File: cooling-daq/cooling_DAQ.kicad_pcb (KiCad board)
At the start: 2 copper layers, 30 x 50 mm, 51 parts, among them J1 Conn_02x10_Odd_Even, J7 USB_C_Receptacle_USB2.0_16P, Q1 2N7002, Q2 2N7002, SW1 SW_SPST, U1 STM32F103C8Tx, U2 AP2204K-ADJ, U3 AP2204K-ADJ, U4 SN65HVD256D, Y1 8M, Y2 32.768k

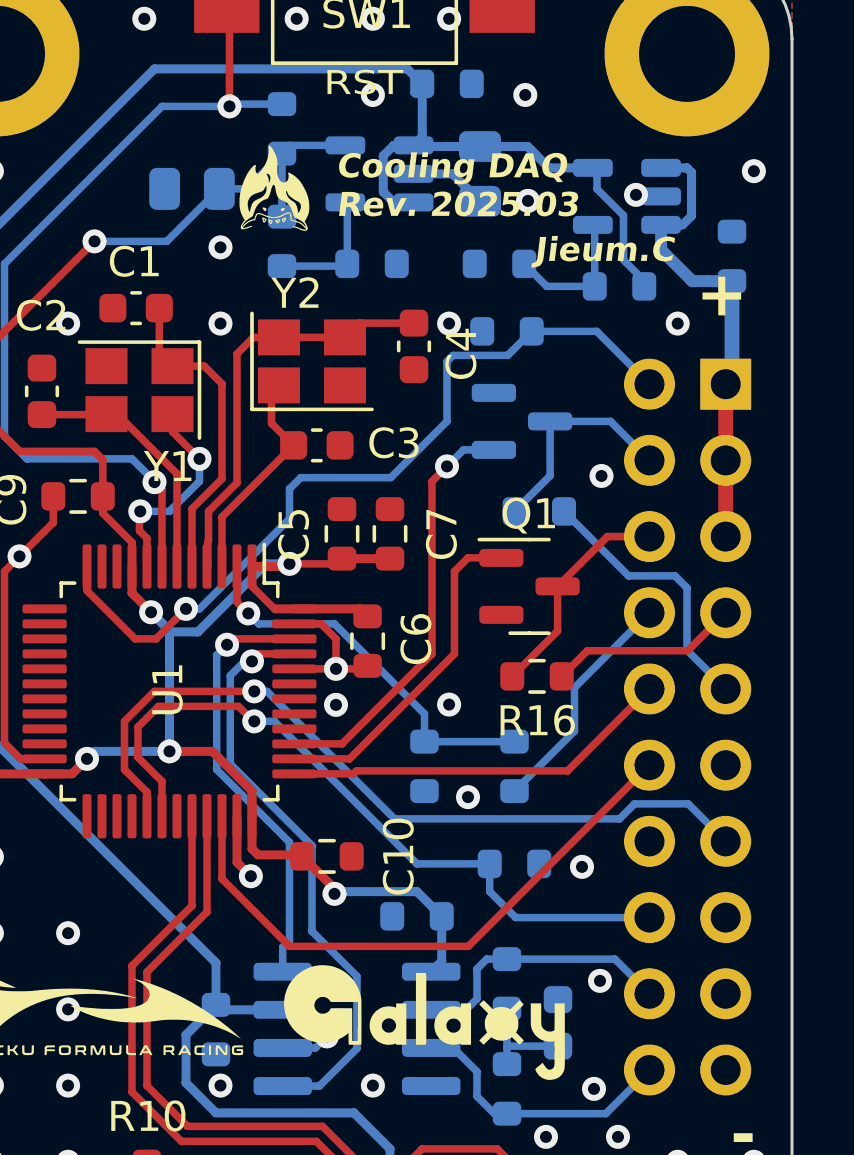
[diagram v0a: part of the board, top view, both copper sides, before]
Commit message: fix CAN IC, modify pump_PWR, fix Cu length label
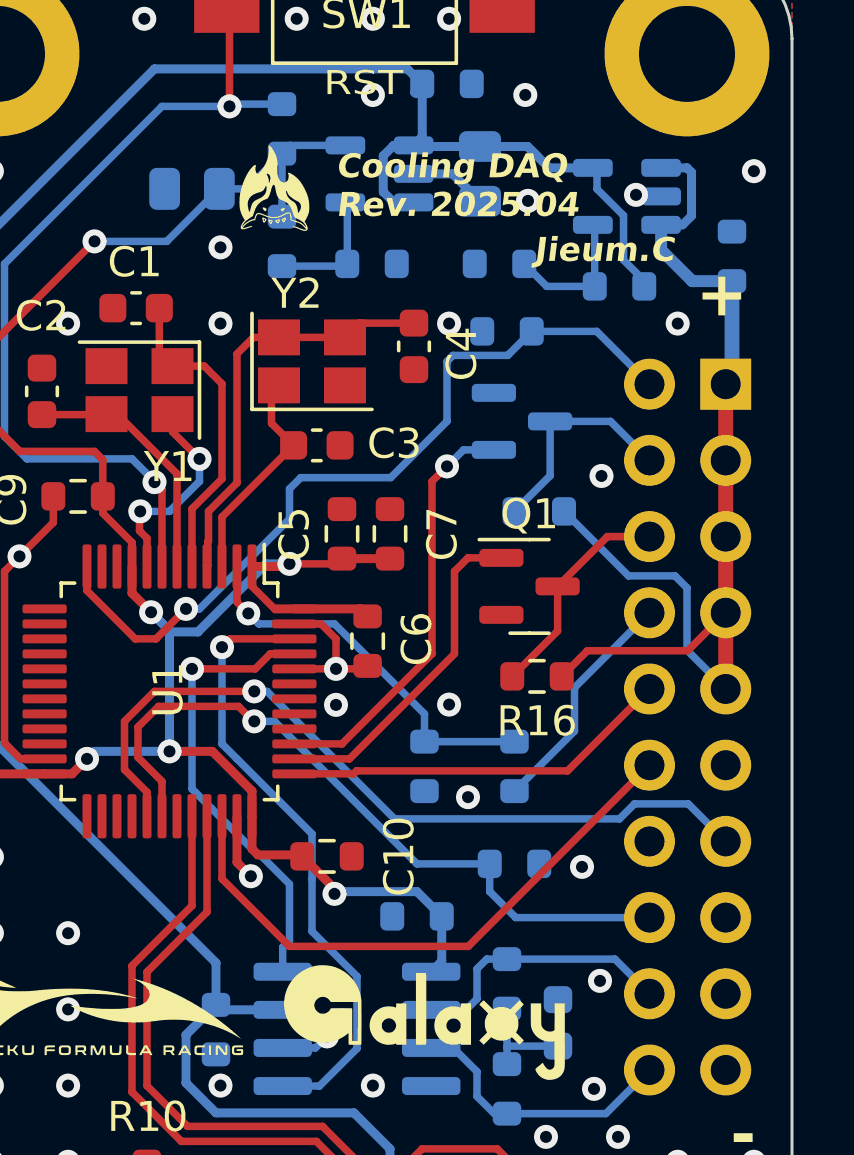
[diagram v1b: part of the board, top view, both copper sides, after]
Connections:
- J1 pad 7: PUMP_PWR -> VDC
- J1 pad 9: FAN_PWR -> VDC
- R14 pad 2: FAN_PWR -> VDC
- R16 pad 2: PUMP_PWR -> VDC
- U1 pad 45: CAN_TX -> CAN_RX
- U1 pad 46: CAN_RX -> CAN_TX
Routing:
- net VDC: track 15.9 -> 36.4 mm
- net FAN_PWR: track 9.06 -> 0.00 mm
- net PUMP_PWR: track 6.34 -> 0.00 mm
- net CAN_TX: track 19.6 -> 20.8 mm
- net CAN_RX: track 14.5 -> 15.2 mm
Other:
- board text added: "Cooling DAQ Rev. 2025.04"
- board text removed: "Cooling DAQ Rev. 2025.03"

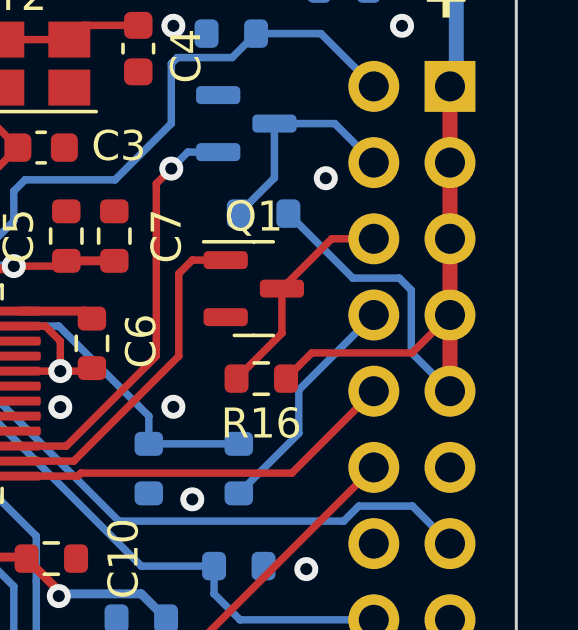
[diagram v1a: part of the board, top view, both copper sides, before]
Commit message: recover PUMP_PWR
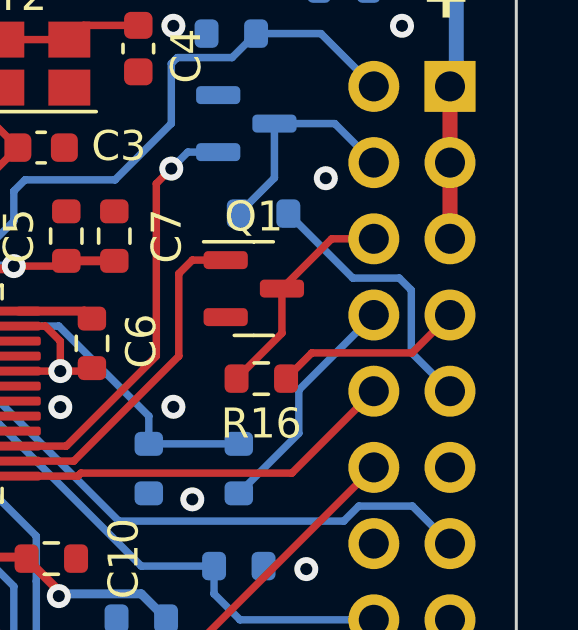
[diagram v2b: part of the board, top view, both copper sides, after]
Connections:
- J1 pad 7: VDC -> PUMP_PWR
- J1 pad 9: VDC -> FAN_PWR
- R14 pad 2: VDC -> FAN_PWR
- R16 pad 2: VDC -> PUMP_PWR
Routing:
- net VDC: track 36.4 -> 15.9 mm
- net FAN_PWR: track 0.00 -> 9.06 mm
- net PUMP_PWR: track 0.00 -> 6.34 mm
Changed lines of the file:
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@@
   (net 56 "unconnected-(J1-Pin_11-Pad11)")
   (net 57 "unconnected-(J1-Pin_14-Pad14)")
+  (net 58 "PUMP_PWR")
+  (net 59 "FAN_PWR")
   (footprint "MountingHole:MountingHole_3.2mm_M3_ISO14580_Pad" (layer "F.Cu")
     (at 158.5 140.5)
@@
       (net 54 "PUMP_PWM") (pintype "passive"))
     (pad "2" smd roundrect (at 0.825 0) (size 0.8 0.95) (layers "F.Cu" "F.Paste" "F.Mask") (roundrect_rratio 0.25)
-      (net 7 "VDC") (pintype "passive"))
+      (net 58 "PUMP_PWR") (pintype "passive"))
     (model "${KICAD6_3DMODEL_DIR}/Resistor_SMD.3dshapes/R_0603_1608Metric.wrl"
       (offset (xyz 0 0 0))
@@
       (net 54 "PUMP_PWM") (pinfunction "Pin_6") (pintype "passive"))
     (pad "7" thru_hole oval (at 0 -7.62 180) (size 1.7 1.7) (drill 1) (layers "*.Cu" "*.Mask")
-      (net 7 "VDC") (pinfunction "Pin_7") (pintype "passive"))
+      (net 58 "PUMP_PWR") (pinfunction "Pin_7") (pintype "passive"))
     (pad "8" thru_hole oval (at 2.54 -7.62 180) (size 1.7 1.7) (drill 1) (layers "*.Cu" "*.Mask")
       (net 13 "PT_signal") (pinfunction "Pin_8") (pintype "passive"))
     (pad "9" thru_hole oval (at 0 -10.16 180) (size 1.7 1.7) (drill 1) (layers "*.Cu" "*.Mask")
-      (net 7 "VDC") (pinfunction "Pin_9") (pintype "passive"))
+      (net 59 "FAN_PWR") (pinfunction "Pin_9") (pintype "passive"))
     (pad "10" thru_hole oval (at 2.54 -10.16 180) (size 1.7 1.7) (drill 1) (layers "*.Cu" "*.Mask")
       (net 10 "SYS_JTCK-SWCLK") (pinfunction "Pin_10") (pintype "passive"))
@@
       (net 55 "FAN_PWM") (pintype "passive"))
     (pad "2" smd roundrect (at 0.825 0) (size 0.8 0.95) (layers "B.Cu" "B.Paste" "B.Mask") (roundrect_rratio 0.25)
-      (net 7 "VDC") (pintype "passive"))
+      (net 59 "FAN_PWR") (pintype "passive"))
     (model "${KICAD6_3DMODEL_DIR}/Resistor_SMD.3dshapes/R_0603_1608Metric.wrl"
       (offset (xyz 0 0 0))
@@
   (segment (start 146.75 125.5) (end 146.825 125.425) (width 0.3) (layer "B.Cu") (net 6))
   (segment (start 141.25 120.75) (end 138.75 120.75) (width 0.3) (layer "B.Cu") (net 6))
-  (segment (start 155.180054 117.394946) (end 158.525054 117.394946) (width 0.25) (layer "F.Cu") (net 7))
-  (segment (start 154.325 118.25) (end 155.180054 117.394946) (width 0.25) (layer "F.Cu") (net 7))
-  (segment (start 159.79 116.13) (end 159.79 118.67) (width 0.5) (layer "F.Cu") (net 7))
-  (segment (start 158.525054 117.394946) (end 159.79 116.13) (width 0.25) (layer "F.Cu") (net 7))
-  (segment (start 159.79 113.59) (end 159.79 116.13) (width 0.5) (layer "F.Cu") (net 7))
   (segment (start 159.79 108.51) (end 159.79 113.59) (width 0.5) (layer "F.Cu") (net 7))
   (segment (start 158.65 102.899999) (end 158.349999 103.2) (width 0.3) (layer "B.Cu") (net 7))
   (segment (start 160 105.075) (end 160 108.3) (width 0.5) (layer "B.Cu") (net 7))
   (segment (start 160 108.3) (end 159.79 108.51) (width 0.25) (layer "B.Cu") (net 7))
-  (segment (start 156.55 114.9) (end 158.1 114.9) (width 0.25) (layer "B.Cu") (net 7))
   (segment (start 157.6375 104.0375) (end 158.675 105.075) (width 0.4) (layer "B.Cu") (net 7))
   (segment (start 158.5 101.3) (end 158.65 101.45) (width 0.3) (layer "B.Cu") (net 7))
   (segment (start 158.65 101.45) (end 158.65 102.899999) (width 0.3) (layer "B.Cu") (net 7))
-  (segment (start 158.1 114.9) (end 158.5 115.3) (width 0.25) (layer "B.Cu") (net 7))
-  (segment (start 158.5 117.38) (end 159.79 118.67) (width 0.25) (layer "B.Cu") (net 7))
   (segment (start 158.675 105.075) (end 159.5125 105.075) (width 0.4) (layer "B.Cu") (net 7))
   (segment (start 157.6375 101.3) (end 158.5 101.3) (width 0.3) (layer "B.Cu") (net 7))
   (segment (start 157.6375 103.2) (end 157.6375 104.0375) (width 0.4) (layer "B.Cu") (net 7))
-  (segment (start 154.4 112.75) (end 156.55 114.9) (width 0.25) (layer "B.Cu") (net 7))
   (segment (start 158.349999 103.2) (end 157.6375 103.2) (width 0.3) (layer "B.Cu") (net 7))
-  (segment (start 158.5 115.3) (end 158.5 117.38) (width 0.25) (layer "B.Cu") (net 7))
   (segment (start 159.5125 105.075) (end 160 105.075) (width 0.25) (layer "B.Cu") (net 7))
   (segment (start 148.515 137.315) (end 145.300305 137.315) (width 0.3) (layer "F.Cu") (net 8))
@@
   (segment (start 153.9375 109.75) (end 153.9375 111.5625) (width 0.25) (layer "B.Cu") (net 55))
   (segment (start 155.95 109.75) (end 157.25 111.05) (width 0.25) (layer "B.Cu") (net 55))
+  (segment (start 155.180054 117.394946) (end 158.525054 117.394946) (width 0.25) (layer "F.Cu") (net 58))
+  (segment (start 154.325 118.25) (end 155.180054 117.394946) (width 0.25) (layer "F.Cu") (net 58))
+  (segment (start 158.525054 117.394946) (end 159.79 116.13) (width 0.25) (layer "F.Cu") (net 58))
+  (segment (start 156.55 114.9) (end 158.1 114.9) (width 0.25) (layer "B.Cu") (net 59))
+  (segment (start 158.1 114.9) (end 158.5 115.3) (width 0.25) (layer "B.Cu") (net 59))
+  (segment (start 158.5 117.38) (end 159.79 118.67) (width 0.25) (layer "B.Cu") (net 59))
+  (segment (start 154.4 112.75) (end 156.55 114.9) (width 0.25) (layer "B.Cu") (net 59))
+  (segment (start 158.5 115.3) (end 158.5 117.38) (width 0.25) (layer "B.Cu") (net 59))
   (zone (net 2) (net_name "GND") (layers "F&B.Cu") (hatch edge 0.5)
     (connect_pads (clearance 0.2))

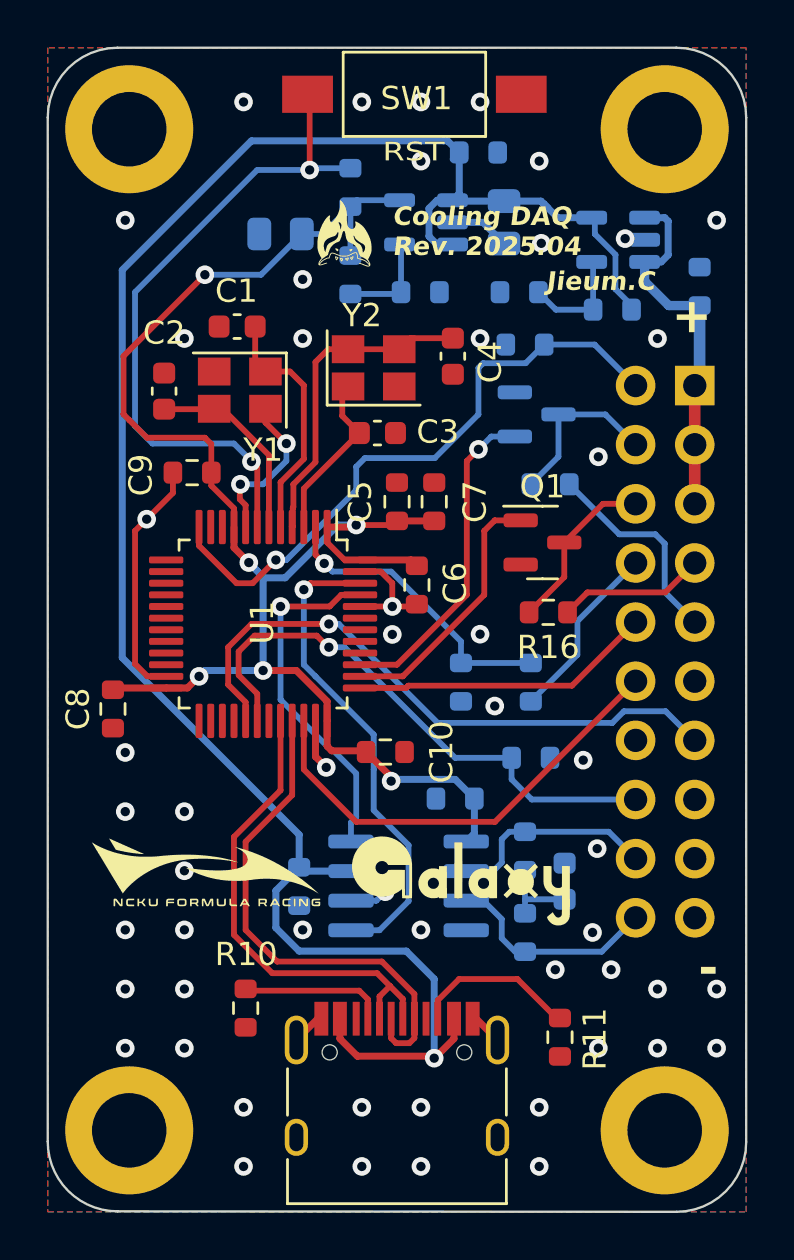
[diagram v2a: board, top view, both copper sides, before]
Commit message: modify: decouple capacitor
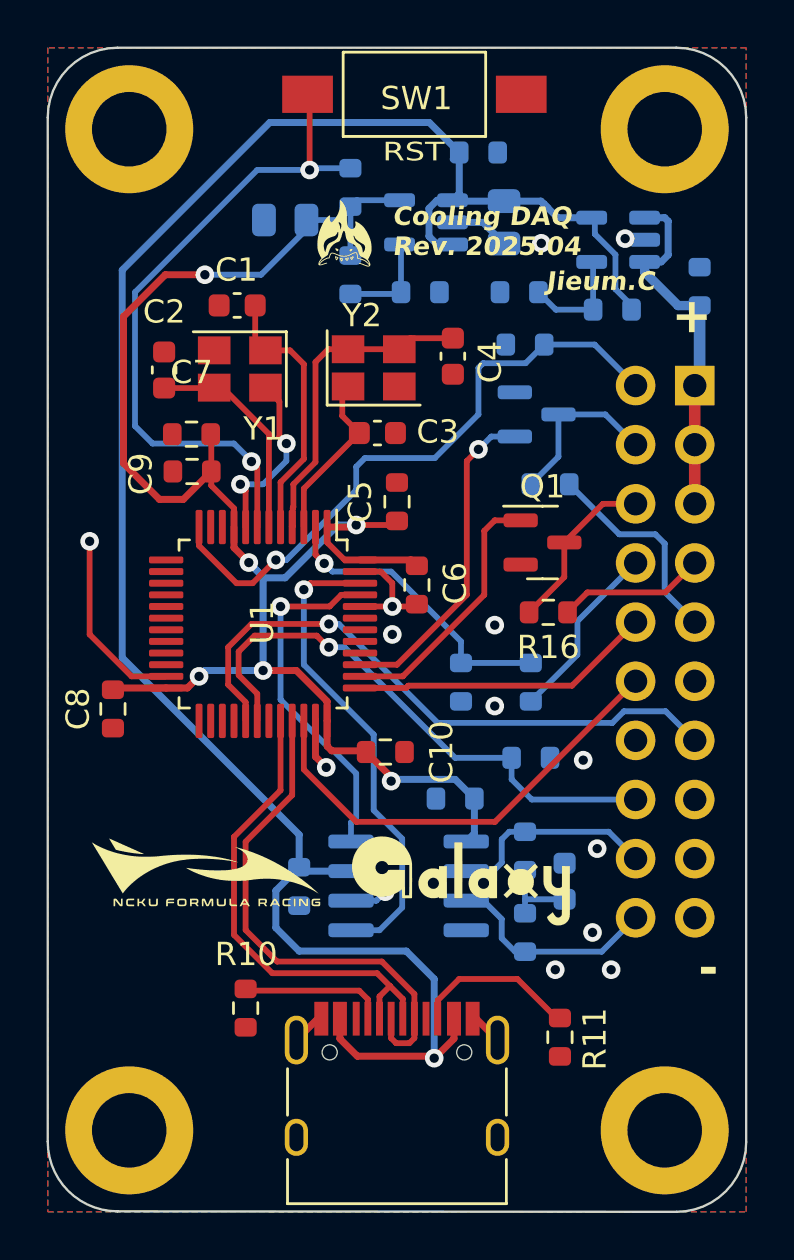
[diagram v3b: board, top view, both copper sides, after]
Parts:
- moved C7 10.8 mm to (138.2, 110.6), turned to 180 degrees
- moved C1 0.91 mm to (140.1, 105.1)
- moved C2 0.91 mm to (137.0, 107.8)
- moved G*** 0.91 mm to (139.6, 117.3)
- moved Y1 0.91 mm to (140.2, 107.8)
- moved C14 0.63 mm to (142.2, 101.4)
- moved C9 0.05 mm to (138.2, 112.2)
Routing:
- net +3V3: track 71.5 -> 73.6 mm
- net GND: track 32.8 -> 31.3 mm, vias 56 -> 16
- net /RCC_OSC_IN: track 10.5 -> 11.4 mm
- net /RCC_OSC_OUT: track 8.41 -> 9.31 mm
- net +5V: track 87.4 -> 88.0 mm

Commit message: v2025.10 :user friendly ver.
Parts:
- added D2: BAT46W-7-F, Diode_SMD:D_SOD-123, B.Cu at (146.0, 140.5)
- added J2: Conn_01x03_Pin, Connector_PinHeader_2.54mm:PinHeader_1x03_P2.54mm_Vertical, F.Cu at (134.8, 128.7)
- added J3: Conn_01x02_Pin, Connector_PinHeader_2.54mm:PinHeader_1x02_P2.54mm_Vertical, F.Cu at (156.0, 135.5)
- added J4: Conn_01x02_Pin, Connector_PinHeader_2.54mm:PinHeader_1x02_P2.54mm_Vertical, F.Cu at (140.8, 96.5)
- added NRST: ~, LED_SMD:LED_0805_2012Metric, F.Cu at (141.1, 102.2)
- added PWR: PWR, LED_SMD:LED_0805_2012Metric, F.Cu at (156.6, 104.8)
- added Q3: Si2301CDS, Package_TO_SOT_SMD:SOT-23, F.Cu at (145.9, 102.7)
- added R15: 4.7k, Resistor_SMD:R_0603_1608Metric, F.Cu at (145.8, 99.2)
- added R17: 1k, Resistor_SMD:R_0603_1608Metric, F.Cu at (155.5, 102.1)
- R11: moved to B.Cu
- moved G*** 11.9 mm to (150.5, 127.2)
- moved G*** 6.95 mm to (151.8, 102.2)
- moved R11 5.00 mm to (150.0, 139.5)
- moved C14 2.26 mm to (142.8, 103.6), turned to -90 degrees
- moved G*** 1.95 mm to (150.8, 131.5)
- moved SW1 1.68 mm to (149.4, 96.2)
- moved C10 1.00 mm to (146.5, 123.2)
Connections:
- net Net-(SW1-B) renamed NRST
- J1 pad 10: SYS_JTCK-SWCLK -> unconnected-(J1-Pin_10-Pad10)
- J1 pad 12: SYS_JTMS-SWDIO -> unconnected-(J1-Pin_12-Pad12)
- J7 pad A4: +5V -> Net-(D2-A)
- J7 pad A9: +5V -> Net-(D2-A)
- J7 pad B4: +5V -> Net-(D2-A)
- J7 pad B9: +5V -> Net-(D2-A)
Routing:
- net Net-(D2-A): track 0.00 -> 10.8 mm, vias 0 -> 1
- net SYS_JTCK-SWCLK: track 13.0 -> 21.9 mm, vias 0 -> 1
- net CAN-: track 9.04 -> 16.5 mm
- net SYS_JTMS-SWDIO: track 19.8 -> 12.8 mm, vias 0 -> 1
- net CAN+: track 9.27 -> 13.3 mm
- net Net-(D1-A): track 0.00 -> 3.58 mm
- net Net-(J7-CC2): track 7.07 -> 10.5 mm, vias 0 -> 1
- net Net-(Q3-G): track 0.00 -> 3.18 mm
- net +3V3: track 73.6 -> 75.9 mm, vias 6 -> 7
- net Net-(D3-A): track 0.00 -> 1.90 mm
- net +5V: track 88.0 -> 86.8 mm
- net NRST: track 29.5 -> 28.8 mm
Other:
- board text added: "5V"
- board text added: "CAN+"
- board text added: "CAN-"
- board text added: "CLK"
- board text added: "Cooling DAQ Rev. 2025.10"
- board text added: "IO"
- board text removed: "Cooling DAQ Rev. 2025.04"
- board text removed: "Jieum.C"
